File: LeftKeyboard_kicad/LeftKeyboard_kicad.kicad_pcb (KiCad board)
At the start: 2 copper layers, 45 parts, among them U1 Arduino_Pro_Micro

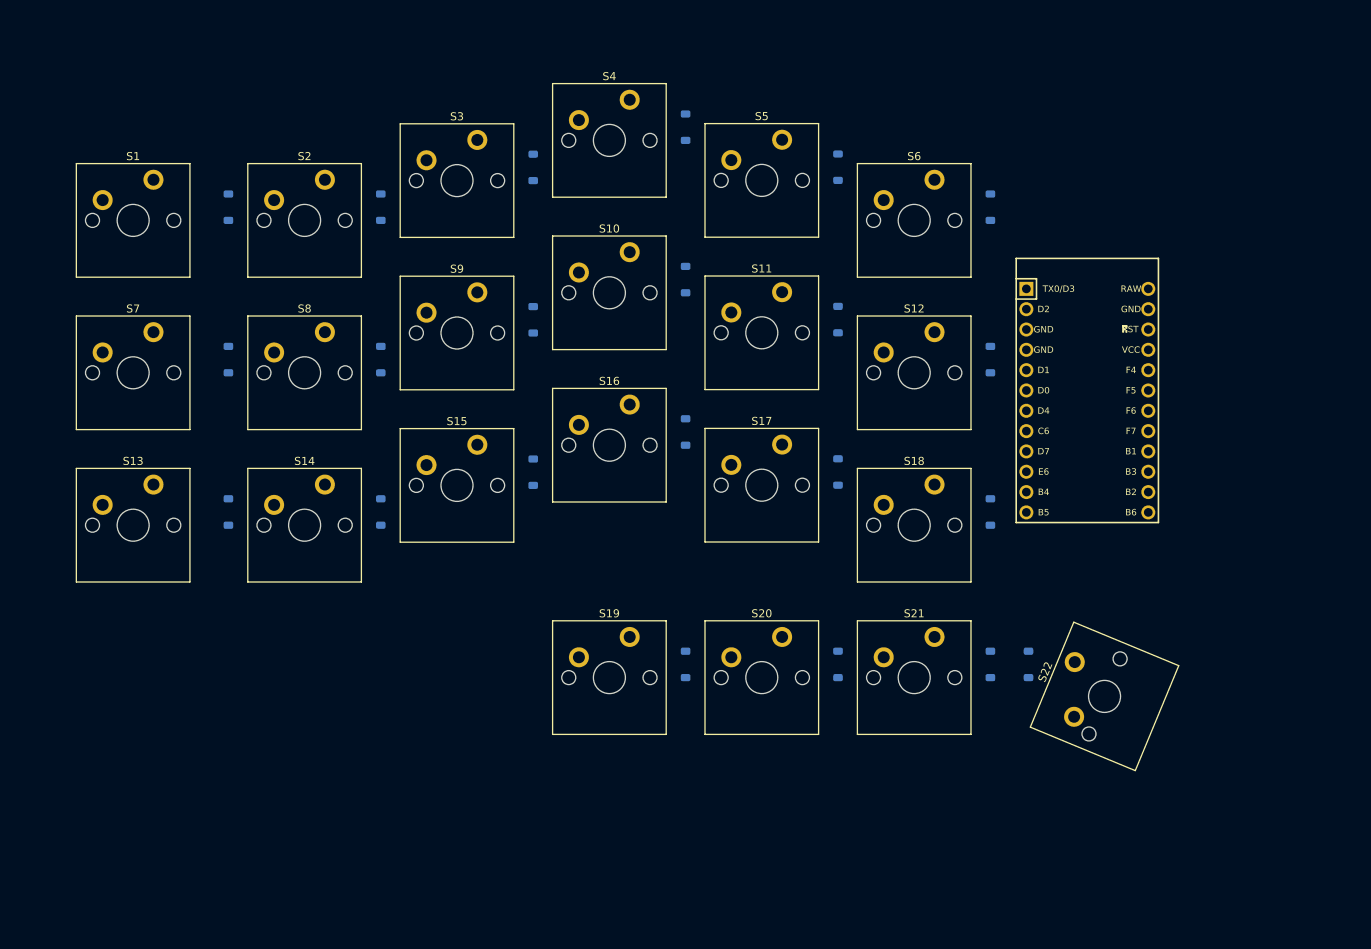
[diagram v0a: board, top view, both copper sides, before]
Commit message: Routed the keyboard
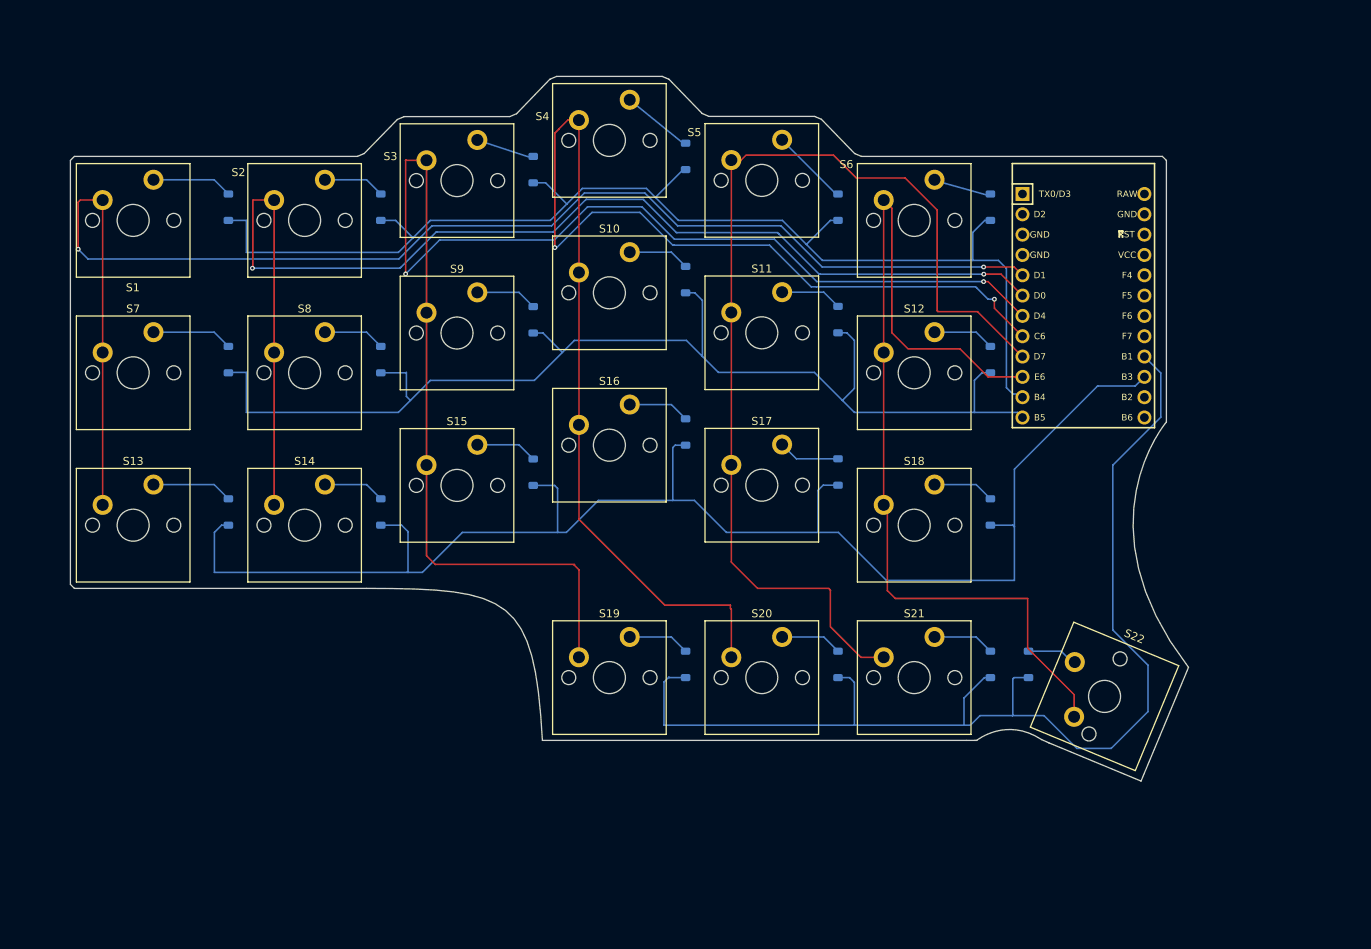
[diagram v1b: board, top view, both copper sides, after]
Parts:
- moved U1 11.9 mm to (156.6, 70.2)
- moved D5 5.00 mm to (125.9, 57.9)
- moved D4 3.65 mm to (106.8, 51.5)
- moved D3 0.27 mm to (87.8, 53.2)
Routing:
- net /Row3: track 0.00 -> 187.3 mm
- net /Col3: track 0.00 -> 183.3 mm, vias 0 -> 2
- net /Col1: track 0.00 -> 173.4 mm, vias 0 -> 2
- net /Col4: track 0.00 -> 165.2 mm, vias 0 -> 2
- net /Col2: track 0.00 -> 154.1 mm, vias 0 -> 2
- net /Row1: track 0.00 -> 153.3 mm
- net /Row4: track 0.00 -> 144.6 mm
- net /Row2: track 0.00 -> 142.8 mm
- net /Col5: track 0.00 -> 131.4 mm
- net /Col6: track 0.00 -> 120.8 mm
- net Net-(D7-A): track 0.00 -> 10.1 mm
- net Net-(D13-A): track 0.00 -> 10.1 mm
- net Net-(D1-A): track 0.00 -> 10.1 mm
- net Net-(D9-A): track 0.00 -> 7.72 mm
- net Net-(D15-A): track 0.00 -> 7.72 mm
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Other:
- board outline added: 139.8 x 88.1 mm

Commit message: finish Left PCB, starting right
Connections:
- U1 pad 3: unconnected-(U1-GND-Pad3) -> /GND
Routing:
- net /Col3: track 183.3 -> 178.5 mm
- net /Row3: track 187.3 -> 191.7 mm
- net /GND: vias 0 -> 19
- added copper zone on B.Cu, net /GND
- added copper zone on F.Cu, net /GND
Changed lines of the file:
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@@
 	(net 38 "unconnected-(U1-16{slash}PB2-Pad14)")
 	(net 39 "unconnected-(U1-A1{slash}PF6-Pad18)")
-	(net 40 "unconnected-(U1-GND-Pad3)")
+	(net 40 "/GND")
 	(net 41 "unconnected-(U1-RST-Pad22)")
 	(net 42 "unconnected-(U1-VCC-Pad21)")
@@
 			(layers "*.Cu" "*.SilkS" "*.Mask")
 			(remove_unused_layers no)
-			(net 40 "unconnected-(U1-GND-Pad3)")
+			(net 40 "/GND")
 			(pinfunction "GND")
 			(pintype "input")
@@
 	)
 	(segment
+		(start 150.68875 80.23125)
+		(end 163.04875 80.23125)
+		(width 0.2)
+		(layer "B.Cu")
+		(net 16)
+	)
+	(segment
 		(start 107.93875 94.53125)
 		(end 111.93875 98.53125)
@@
 	)
 	(segment
+		(start 163.04875 80.23125)
+		(end 164.18875 79.09125)
+		(width 0.2)
+		(layer "B.Cu")
+		(net 16)
+	)
+	(segment
 		(start 125.88875 92.63125)
 		(end 124.03875 92.63125)
@@
 	)
 	(segment
+		(start 147.93875 97.83125)
+		(end 147.93875 88.43125)
+		(width 0.2)
+		(layer "B.Cu")
+		(net 16)
+	)
+	(segment
 		(start 111.93875 98.53125)
 		(end 123.38875 98.53125)
@@
 	)
 	(segment
+		(start 150.18875 86.18125)
+		(end 150.18875 80.73125)
+		(width 0.2)
+		(layer "B.Cu")
+		(net 16)
+	)
+	(segment
 		(start 49.68875 97.63125)
 		(end 48.83875 97.63125)
@@
 	)
 	(segment
+		(start 147.93875 88.43125)
+		(end 150.18875 86.18125)
+		(width 0.2)
+		(layer "B.Cu")
+		(net 16)
+	)
+	(segment
 		(start 72.13875 103.53125)
 		(end 73.93875 103.53125)
@@
 	)
 	(segment
+		(start 150.18875 80.73125)
+		(end 150.68875 80.23125)
+		(width 0.2)
+		(layer "B.Cu")
+		(net 16)
+	)
+	(segment
 		(start 87.78875 92.65625)
 		(end 90.46375 92.65625)
@@
 	)
 	(segment
-		(start 163.04875 80.23125)
-		(end 164.18875 79.09125)
-		(width 0.2)
-		(layer "B.Cu")
-		(net 16)
-	)
-	(segment
 		(start 144.93875 97.63125)
 		(end 147.73875 97.63125)
@@
 	)
 	(segment
-		(start 158.33875 80.23125)
-		(end 163.04875 80.23125)
-		(width 0.2)
-		(layer "B.Cu")
-		(net 16)
-	)
-	(segment
 		(start 71.33875 97.63125)
 		(end 72.13875 98.43125)
@@
 	)
 	(segment
-		(start 147.93875 97.83125)
-		(end 147.93875 90.63125)
-		(width 0.2)
-		(layer "B.Cu")
-		(net 16)
-	)
-	(segment
 		(start 48.83875 97.63125)
 		(end 47.93875 98.53125)
@@
 	)
 	(segment
-		(start 147.93875 90.63125)
-		(end 158.33875 80.23125)
-		(width 0.2)
-		(layer "B.Cu")
-		(net 16)
-	)
-	(segment
 		(start 61.75375 92.55125)
 		(end 66.95875 92.55125)
@@
 	)
 	(segment
-		(start 93.50375 103.19625)
-		(end 93.50375 114.14125)
+		(start 84.68875 102.53125)
+		(end 93.50375 111.34625)
 		(width 0.2)
 		(layer "F.Cu")
@@
 	)
 	(segment
-		(start 75.53875 102.53125)
-		(end 92.93875 102.53125)
+		(start 74.45375 101.44625)
+		(end 75.53875 102.53125)
 		(width 0.2)
 		(layer "F.Cu")
@@
 	)
 	(segment
-		(start 74.45375 101.44625)
-		(end 75.53875 102.53125)
+		(start 144.08875 67.18125)
+		(end 144.65875 67.18125)
 		(width 0.2)
 		(layer "F.Cu")
@@
 	)
 	(segment
-		(start 144.08875 67.18125)
-		(end 144.65875 67.18125)
+		(start 75.53875 102.53125)
+		(end 84.68875 102.53125)
 		(width 0.2)
 		(layer "F.Cu")
@@
 	)
 	(segment
-		(start 71.83875 52.00625)
-		(end 71.83875 62.65625)
-		(width 0.2)
-		(layer "F.Cu")
-		(net 29)
-	)
-	(segment
-		(start 71.86375 51.98125)
-		(end 71.83875 52.00625)
+		(start 93.50375 111.34625)
+		(end 93.50375 114.14125)
 		(width 0.2)
 		(layer "F.Cu")
@@
 	)
 	(segment
-		(start 92.93875 102.63125)
-		(end 93.50375 103.19625)
+		(start 71.83875 52.00625)
+		(end 71.83875 62.65625)
 		(width 0.2)
 		(layer "F.Cu")
@@
 	)
 	(segment
-		(start 92.93875 102.53125)
-		(end 92.93875 102.63125)
+		(start 71.86375 51.98125)
+		(end 71.83875 52.00625)
 		(width 0.2)
 		(layer "F.Cu")
@@
 		(net 32)
 	)
+	(via
+		(at 47.73875 68.88125)
+		(size 0.6)
+		(drill 0.3)
+		(layers "F.Cu" "B.Cu")
+		(free yes)
+		(net 40)
+	)
+	(via
+		(at 125.73875 85.48125)
+		(size 0.6)
+		(drill 0.3)
+		(layers "F.Cu" "B.Cu")
+		(free yes)
+		(net 40)
+	)
+	(via
+		(at 135.38875 63.08125)
+		(size 0.6)
+		(drill 0.3)
+		(layers "F.Cu" "B.Cu")
+		(free yes)
+		(net 40)
+	)
+	(via
+		(at 67.68875 68.88125)
+		(size 0.6)
+		(drill 0.3)
+		(layers "F.Cu" "B.Cu")
+		(free yes)
+		(net 40)
+	)
+	(via
+		(at 107.03875 102.93125)
+		(size 0.6)
+		(drill 0.3)
+		(layers "F.Cu" "B.Cu")
+		(free yes)
+		(net 40)
+	)
+	(via
+		(at 107.48875 57.33125)
+		(size 0.6)
+		(drill 0.3)
+		(layers "F.Cu" "B.Cu")
+		(free yes)
+		(net 40)
+	)
+	(via
+		(at 154.78875 91.33125)
+		(size 0.6)
+		(drill 0.3)
+		(layers "F.Cu" "B.Cu")
+		(free yes)
+		(net 40)
+	)
+	(via
+		(at 154.58875 104.78125)
+		(size 0.6)
+		(drill 0.3)
+		(layers "F.Cu" "B.Cu")
+		(free yes)
+		(net 40)
+	)
+	(via
+		(at 144.98875 53.58125)
+		(size 0.6)
+		(drill 0.3)
+		(layers "F.Cu" "B.Cu")
+		(free yes)
+		(net 40)
+	)
+	(via
+		(at 91.48875 103.88125)
+		(size 0.6)
+		(drill 0.3)
+		(layers "F.Cu" "B.Cu")
+		(free yes)
+		(net 40)
+	)
+	(via
+		(at 87.68875 84.08125)
+		(size 0.6)
+		(drill 0.3)
+		(layers "F.Cu" "B.Cu")
+		(free yes)
+		(net 40)
+	)
+	(via
+		(at 87.68875 65.43125)
+		(size 0.6)
+		(drill 0.3)
+		(layers "F.Cu" "B.Cu")
+		(free yes)
+		(net 40)
+	)
+	(via
+		(at 46.98875 88.18125)
+		(size 0.6)
+		(drill 0.3)
+		(layers "F.Cu" "B.Cu")
+		(free yes)
+		(net 40)
+	)
+	(via
+		(at 106.38875 78.53125)
+		(size 0.6)
+		(drill 0.3)
+		(layers "F.Cu" "B.Cu")
+		(free yes)
+		(net 40)
+	)
+	(via
+		(at 145.13875 119.28125)
+		(size 0.6)
+		(drill 0.3)
+		(layers "F.Cu" "B.Cu")
+		(free yes)
+		(net 40)
+	)
+	(via
+		(at 162.73875 109.33125)
+		(size 0.6)
+		(drill 0.3)
+		(layers "F.Cu" "B.Cu")
+		(free yes)
+		(net 40)
+	)
+	(via
+		(at 145.38875 62.28125)
+		(size 0.6)
+		(drill 0.3)
+		(layers "F.Cu" "B.Cu")
+		(free yes)
+		(net 40)
+	)
+	(via
+		(at 125.33875 102.53125)
+		(size 0.6)
+		(drill 0.3)
+		(layers "F.Cu" "B.Cu")
+		(free yes)
+		(net 40)
+	)
+	(via
+		(at 67.93875 88.38125)
+		(size 0.6)
+		(drill 0.3)
+		(layers "F.Cu" "B.Cu")
+		(free yes)
+		(net 40)
+	)
+	(zone
+		(net 40)
+		(net_name "/GND")
+		(layers "F.Cu" "B.Cu")
+		(hatch edge 0.5)
+		(connect_pads
+			(clearance 0.5)
+		)
+		(min_thickness 0.25)
+		(filled_areas_thickness no)
+		(fill yes
+			(thermal_gap 0.5)
+			(thermal_bridge_width 0.5)
+		)
+		(polygon
+			(pts
+				(xy 23.13875 42.73125) (xy 190.48875 33.98125) (xy 168.08875 148.63125) (xy 23.13875 116.73125)
+			)
+		)
+	)
+	(zone
+		(net 0)
+		(net_name "")
+		(layers "F.Cu" "B.Cu")
+		(hatch edge 0.5)
+		(connect_pads
+			(clearance 0)
+		)
+		(min_thickness 0.25)
+		(filled_areas_thickness no)
+		(keepout
+			(tracks not_allowed)
+			(vias not_allowed)
+			(pads not_allowed)
+			(copperpour not_allowed)
+			(footprints allowed)
+		)
+		(placement
+			(enabled no)
+			(sheetname "/")
+		)
+		(fill
+			(thermal_gap 0.5)
+			(thermal_bridge_width 0.5)
+		)
+		(polygon
+			(pts
+				(xy 150.28875 80.88125) (xy 150.98875 80.48125) (xy 162.98875 80.48125) (xy 162.98875 86.51125)
+				(xy 150.415716 86.670908)
+			)
+		)
+	)
 	(group ""

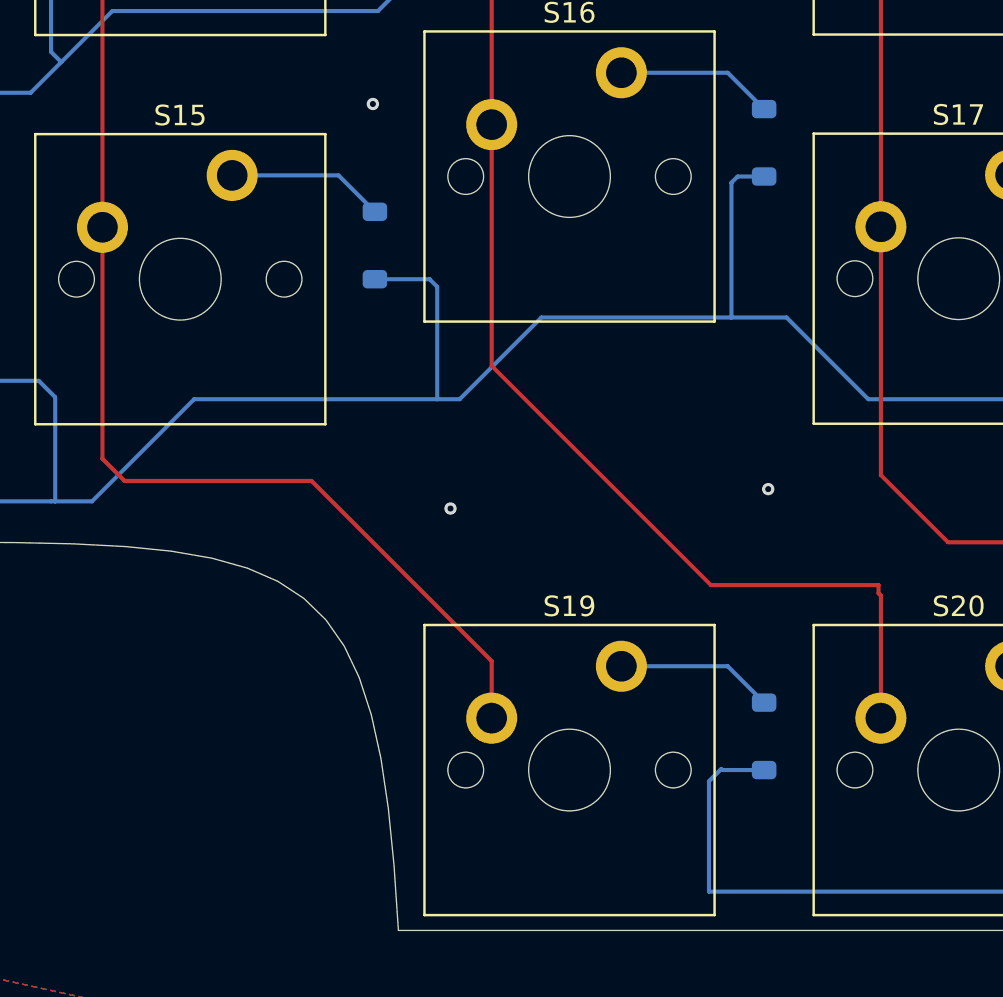
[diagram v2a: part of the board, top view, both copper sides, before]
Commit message: Finished Right Keyboard PCB
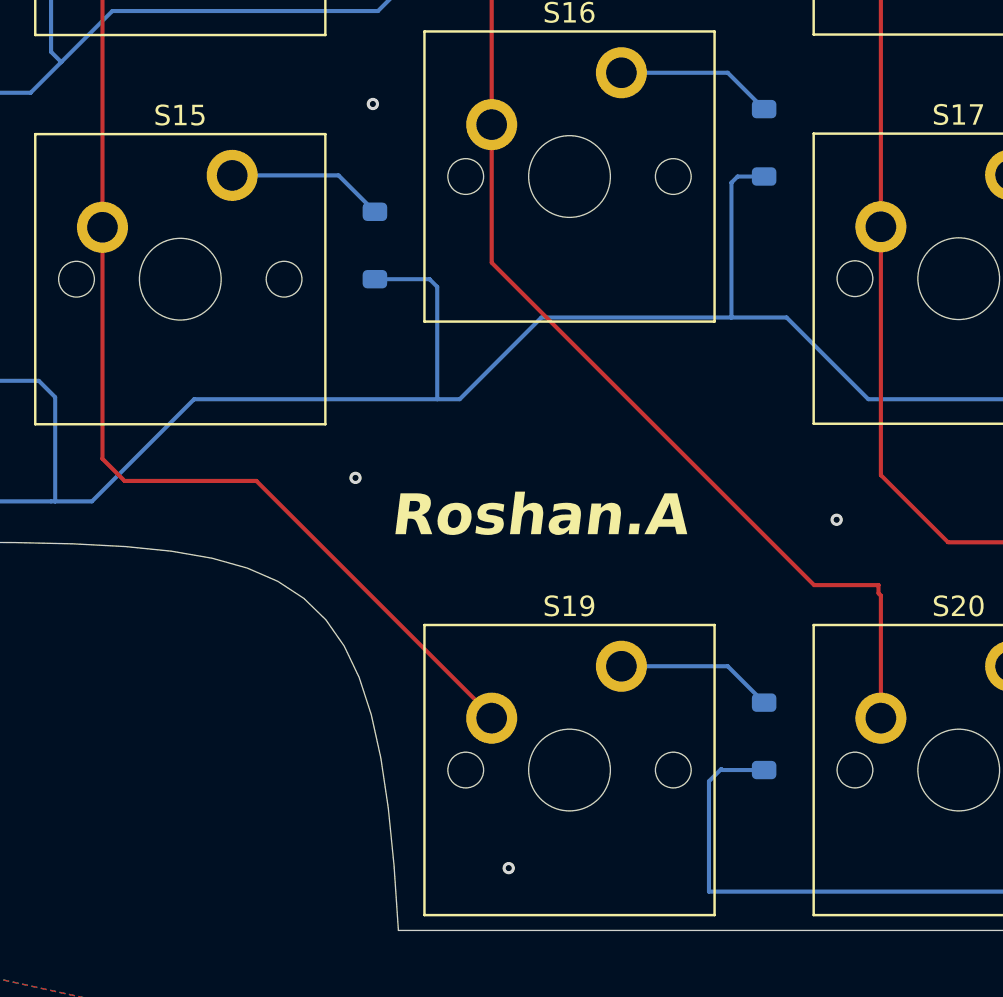
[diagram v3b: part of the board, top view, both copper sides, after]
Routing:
- net /Col4: track 165.2 -> 162.2 mm
- net /Col3: track 178.5 -> 176.9 mm
- net /GND: vias 19 -> 20
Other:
- board text added: "Roshan.A"
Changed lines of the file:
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@@
 		(layer "Edge.Cuts")
+	)
+	(gr_text "Roshan.A"
+		(at 88.53875 105.38125 0)
+		(layer "F.SilkS")
+		(effects
+			(font
+				(size 2 2)
+				(thickness 0.25)
+				(bold yes)
+				(italic yes)
+			)
+			(justify left bottom)
+		)
 	)
 	(segment
@@
 	)
 	(segment
-		(start 84.68875 102.53125)
-		(end 93.50375 111.34625)
-		(width 0.2)
-		(layer "F.Cu")
-		(net 29)
-	)
-	(segment
 		(start 74.45375 101.44625)
 		(end 75.53875 102.53125)
@@
 	)
 	(segment
+		(start 81.98875 102.53125)
+		(end 93.50375 114.04625)
+		(width 0.2)
+		(layer "F.Cu")
+		(net 29)
+	)
+	(segment
 		(start 74.45375 90.11625)
 		(end 74.45375 101.44625)
@@
 	)
 	(segment
-		(start 75.53875 102.53125)
-		(end 84.68875 102.53125)
-		(width 0.2)
-		(layer "F.Cu")
-		(net 29)
-	)
-	(segment
 		(start 74.45375 52.01625)
 		(end 71.89875 52.01625)
@@
 	)
 	(segment
+		(start 75.53875 102.53125)
+		(end 81.98875 102.53125)
+		(width 0.2)
+		(layer "F.Cu")
+		(net 29)
+	)
+	(segment
 		(start 144.65875 67.18125)
 		(end 148.94875 71.47125)
@@
 	)
 	(segment
-		(start 93.50375 111.34625)
-		(end 93.50375 114.14125)
-		(width 0.2)
-		(layer "F.Cu")
-		(net 29)
-	)
-	(segment
 		(start 71.83875 52.00625)
 		(end 71.83875 62.65625)
+		(width 0.2)
+		(layer "F.Cu")
+		(net 29)
+	)
+	(segment
+		(start 93.50375 114.04625)
+		(end 93.50375 114.14125)
 		(width 0.2)
 		(layer "F.Cu")
@@
 	)
 	(segment
-		(start 93.50375 96.89625)
-		(end 104.23875 107.63125)
+		(start 112.43875 107.63125)
+		(end 112.43875 108.03125)
 		(width 0.2)
 		(layer "F.Cu")
@@
 	)
 	(segment
+		(start 93.50375 66.04125)
+		(end 93.50375 85.09125)
+		(width 0.2)
+		(layer "F.Cu")
+		(net 30)
+	)
+	(segment
+		(start 90.96375 48.13125)
+		(end 90.96375 48.15625)
+		(width 0.2)
+		(layer "F.Cu")
+		(net 30)
+	)
+	(segment
+		(start 92.10375 46.99125)
+		(end 90.96375 48.13125)
+		(width 0.2)
+		(layer "F.Cu")
+		(net 30)
+	)
+	(segment
+		(start 93.50375 91.84625)
+		(end 109.28875 107.63125)
+		(width 0.2)
+		(layer "F.Cu")
+		(net 30)
+	)
+	(segment
+		(start 93.50375 46.99125)
+		(end 93.50375 66.04125)
+		(width 0.2)
+		(layer "F.Cu")
+		(net 30)
+	)
+	(segment
+		(start 93.50375 85.09125)
+		(end 93.50375 91.84625)
+		(width 0.2)
+		(layer "F.Cu")
+		(net 30)
+	)
+	(segment
+		(start 145.43875 70.50125)
+		(end 148.94875 74.01125)
+		(width 0.2)
+		(layer "F.Cu")
+		(net 30)
+	)
+	(segment
+		(start 93.50375 46.99125)
+		(end 92.10375 46.99125)
+		(width 0.2)
+		(layer "F.Cu")
+		(net 30)
+	)
+	(segment
+		(start 112.43875 108.03125)
+		(end 112.55375 108.14625)
+		(width 0.2)
+		(layer "F.Cu")
+		(net 30)
+	)
+	(segment
 		(start 112.55375 108.14625)
 		(end 112.55375 114.14125)
@@
 	)
 	(segment
-		(start 93.50375 66.04125)
-		(end 93.50375 85.09125)
-		(width 0.2)
-		(layer "F.Cu")
-		(net 30)
-	)
-	(segment
-		(start 93.50375 85.09125)
-		(end 93.50375 96.89625)
-		(width 0.2)
-		(layer "F.Cu")
-		(net 30)
-	)
-	(segment
-		(start 90.96375 48.13125)
-		(end 90.96375 48.15625)
-		(width 0.2)
-		(layer "F.Cu")
-		(net 30)
-	)
-	(segment
-		(start 92.10375 46.99125)
-		(end 90.96375 48.13125)
-		(width 0.2)
-		(layer "F.Cu")
-		(net 30)
-	)
-	(segment
-		(start 93.50375 46.99125)
-		(end 93.50375 66.04125)
-		(width 0.2)
-		(layer "F.Cu")
-		(net 30)
-	)
-	(segment
-		(start 112.43875 107.63125)
-		(end 112.43875 108.03125)
-		(width 0.2)
-		(layer "F.Cu")
-		(net 30)
-	)
-	(segment
-		(start 104.23875 107.63125)
+		(start 109.28875 107.63125)
 		(end 112.43875 107.63125)
-		(width 0.2)
-		(layer "F.Cu")
-		(net 30)
-	)
-	(segment
-		(start 145.43875 70.50125)
-		(end 148.94875 74.01125)
-		(width 0.2)
-		(layer "F.Cu")
-		(net 30)
-	)
-	(segment
-		(start 93.50375 46.99125)
-		(end 92.10375 46.99125)
 		(width 0.2)
 		(layer "F.Cu")
@@
 		(start 90.48875 48.63125)
 		(end 90.48875 62.93125)
-		(width 0.2)
-		(layer "F.Cu")
-		(net 30)
-	)
-	(segment
-		(start 112.43875 108.03125)
-		(end 112.55375 108.14625)
 		(width 0.2)
 		(layer "F.Cu")
@@
 	)
 	(via
-		(at 107.03875 102.93125)
+		(at 110.38875 104.43125)
 		(size 0.6)
 		(drill 0.3)
@@
 	)
 	(via
-		(at 91.48875 103.88125)
+		(at 86.83875 102.38125)
 		(size 0.6)
 		(drill 0.3)
+		(layers "F.Cu" "B.Cu")
+		(free yes)
+		(net 40)
+	)
+	(via
+		(at 94.33875 121.48125)
+		(size 0.6)
+		(drill 0.3)
